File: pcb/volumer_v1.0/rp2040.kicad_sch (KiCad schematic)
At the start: 27 parts, among them SW1 SW_MEC_5E, SW2 SW_MEC_5E, U3 W25Q128JVS, U4 RP2040, U8 LD1117S33TR, Y2 12Mhz

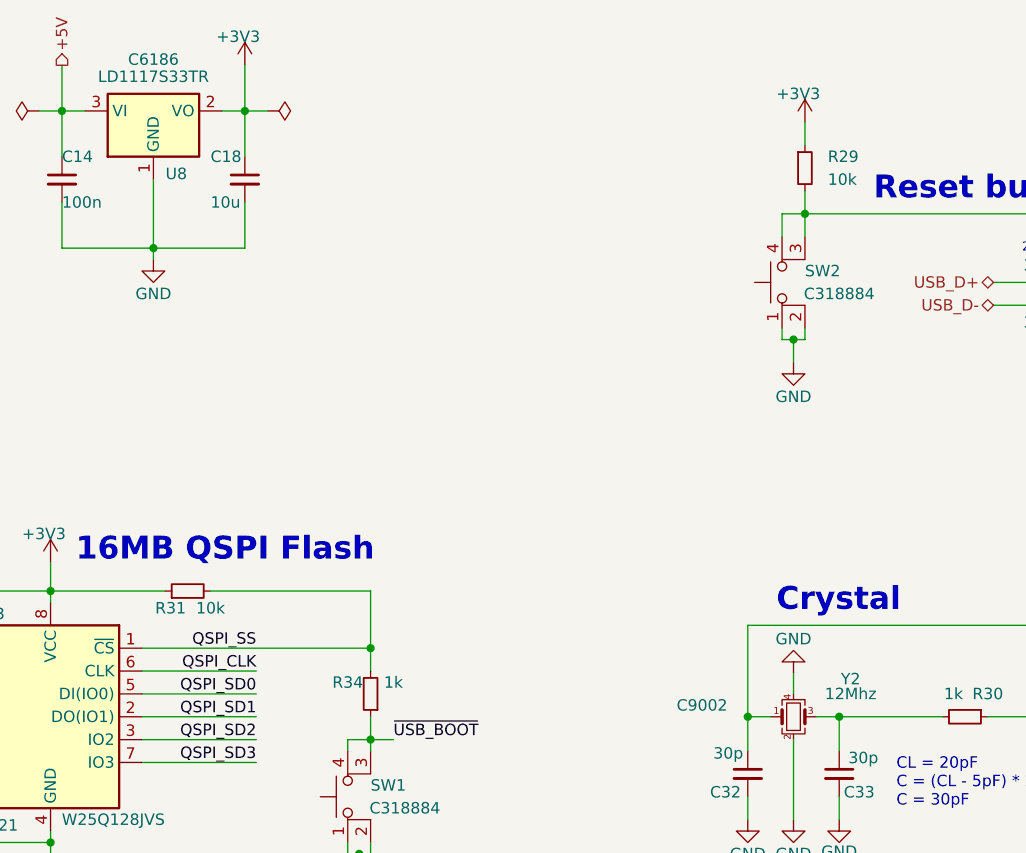
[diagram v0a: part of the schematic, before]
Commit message: Added images
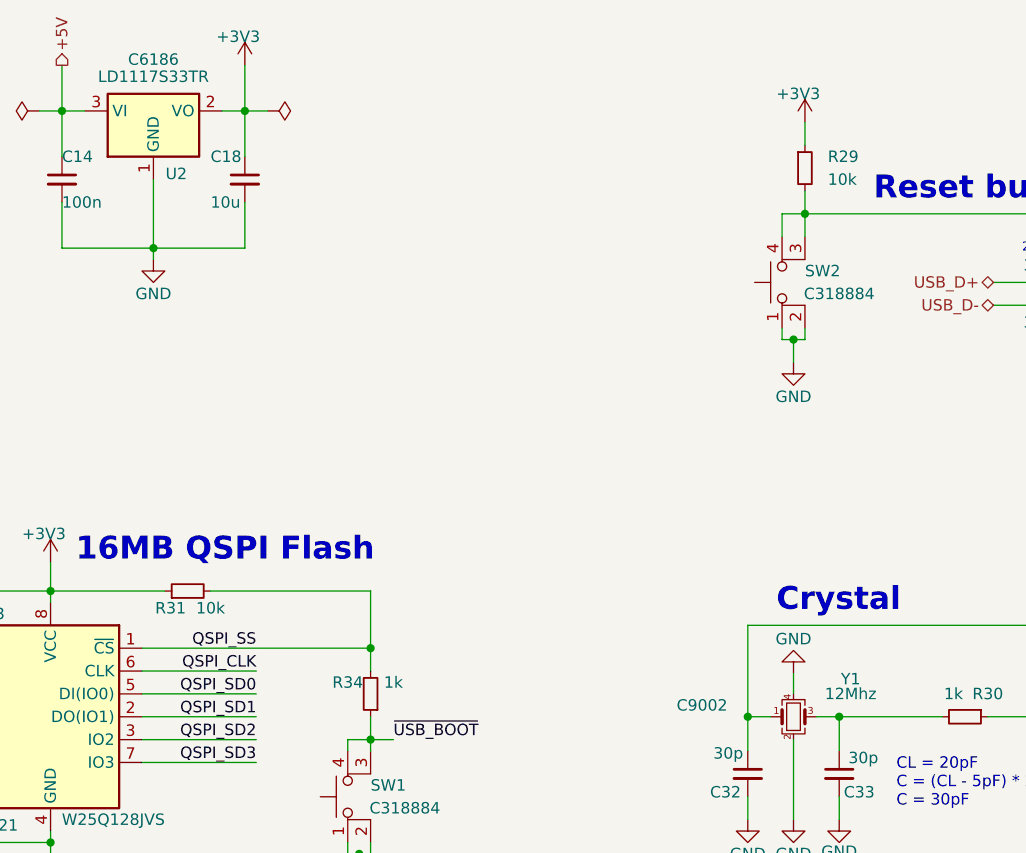
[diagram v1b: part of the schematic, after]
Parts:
- renumbered U8 to U2, Y2 to Y1
